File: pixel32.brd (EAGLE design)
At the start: 42 parts, among them CON1 DS1066-07M-SIDE, CON2 DS1066-07M-SIDE, IC1 STM32F030K6TX-LQFP32(7X7), IC2 ESDA6V1L, IC3 ST3485SOIC8, IC4 MC74VHC1GT125, IC5 MC74VHC1GT125, Q1 FDC6420C

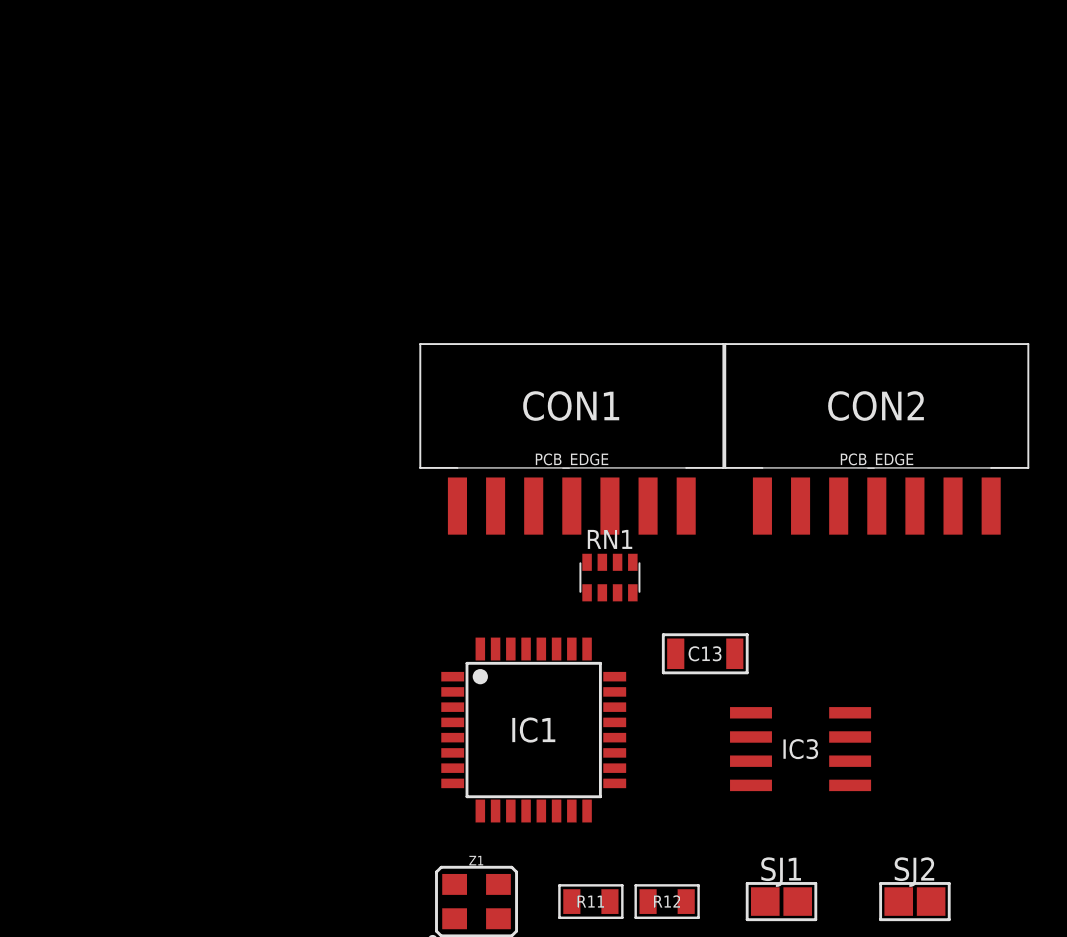
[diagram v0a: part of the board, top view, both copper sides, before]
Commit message: naming fixes pixel8 initial import
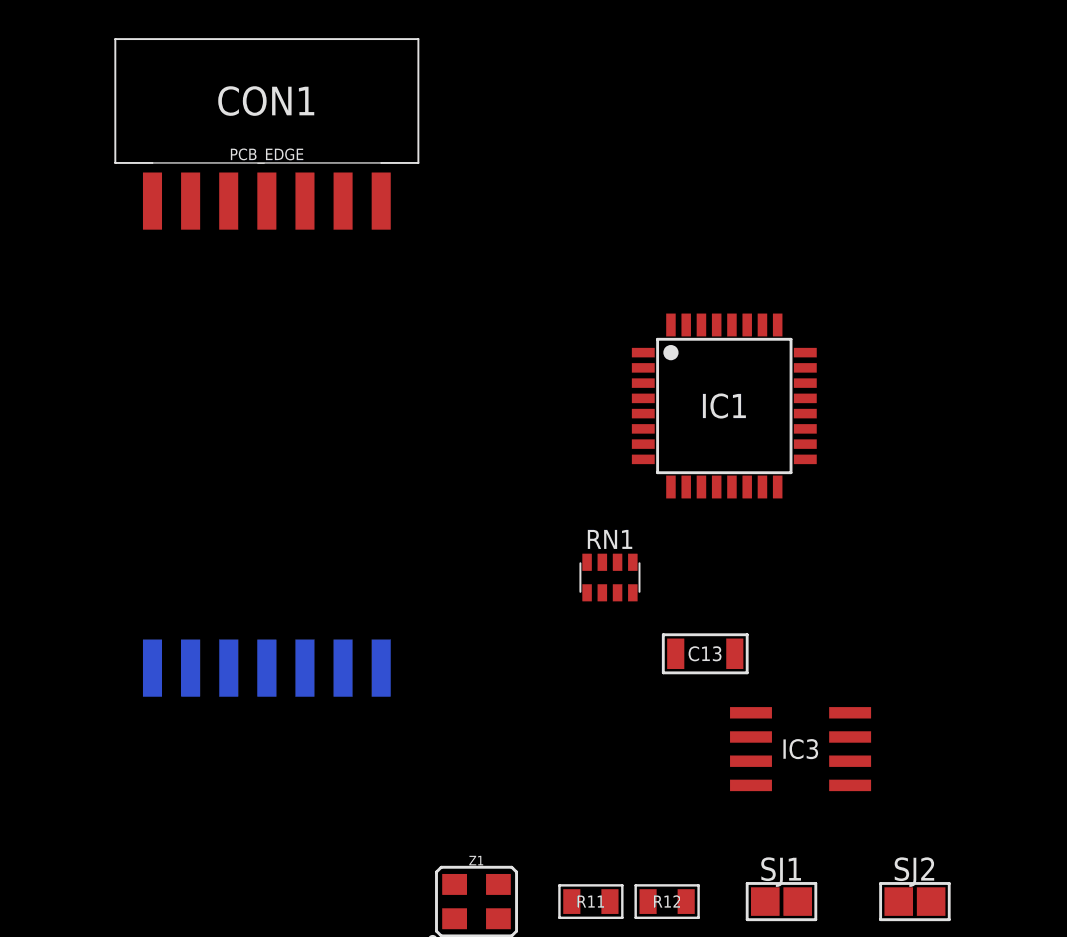
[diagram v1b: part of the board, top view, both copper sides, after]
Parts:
- moved CON2 33.2 mm to (-20.0, -30.0), flipped to the bottom, turned to 180 degrees
- moved CON1 22.6 mm to (-20.0, -5.00)
- moved IC1 19.7 mm to (4.00, -16.0)
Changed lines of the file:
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@@
 </autorouter>
 <elements>
-<element name="IC1" library="pixel_masterlib" package="LQFP32-7X7" value="STM32F030K6TX-LQFP32(7X7)" x="-6" y="-33">
-<attribute name="MANF" value="STMicroelectronics" x="-6" y="-19" size="1.778" layer="27" display="off"/>
-<attribute name="DIGIKEY#" value="497-14046-ND" x="-6" y="-19" size="1.778" layer="27" display="off"/>
-<attribute name="MANF#" value="STM32F030K6T6" x="-6" y="-19" size="1.778" layer="27" display="off"/>
+<element name="IC1" library="pixel_masterlib" package="LQFP32-7X7" value="STM32F030K6TX-LQFP32(7X7)" x="4" y="-16">
+<attribute name="MANF" value="STMicroelectronics" x="4" y="-2" size="1.778" layer="27" display="off"/>
+<attribute name="DIGIKEY#" value="497-14046-ND" x="4" y="-2" size="1.778" layer="27" display="off"/>
+<attribute name="MANF#" value="STM32F030K6T6" x="4" y="-2" size="1.778" layer="27" display="off"/>
 </element>
 <element name="C2" library="rc" package="C0603" value="100 nF" x="-6" y="-46">
@@
 <attribute name="MANF#" value="CX3225GB16000P0HPQCC" x="-8" y="-64" size="1.778" layer="27" display="off"/>
 </element>
-<element name="CON1" library="pixel_masterlib" package="DS1066-08M_SIDE" value="DS1066-07M-SIDE" x="-4" y="-21"/>
-<element name="CON2" library="pixel_masterlib" package="DS1066-08M_SIDE" value="DS1066-07M-SIDE" x="12" y="-21"/>
+<element name="CON1" library="pixel_masterlib" package="DS1066-08M_SIDE" value="DS1066-07M-SIDE" x="-20" y="-5"/>
+<element name="CON2" library="pixel_masterlib" package="DS1066-08M_SIDE" value="DS1066-07M-SIDE" x="-20" y="-30" rot="MR180"/>
 <element name="D1" library="pixel_masterlib" package="SC70_6L" value="SMF05C" x="-10" y="-53">
 <attribute name="MANF" value="Semtech Corporation" x="-9" y="-96" size="1.778" layer="27" display="off"/>
@@
 <wire x1="15.725" y1="-46" x2="12.725" y2="-46" width="0" layer="19" extent="1-1"/>
 <wire x1="18.725" y1="-46" x2="15.725" y2="-46" width="0" layer="19" extent="1-1"/>
-<wire x1="-1.75" y1="-35.8" x2="-1.275" y2="-46" width="0" layer="19" extent="1-1"/>
-<wire x1="-10.25" y1="-33.4" x2="-1.75" y2="-35.8" width="0" layer="19" extent="1-1"/>
-<wire x1="-10.25" y1="-30.2" x2="-10.25" y2="-33.4" width="0" layer="19" extent="1-1"/>
-<wire x1="10.6" y1="-32.095" x2="-1.75" y2="-35.8" width="0" layer="19" extent="1-1"/>
+<wire x1="8.25" y1="-18.8" x2="-1.275" y2="-46" width="0" layer="19" extent="1-1"/>
+<wire x1="-0.25" y1="-16.4" x2="8.25" y2="-18.8" width="0" layer="19" extent="1-1"/>
+<wire x1="-0.25" y1="-13.2" x2="-0.25" y2="-16.4" width="0" layer="19" extent="1-1"/>
+<wire x1="10.6" y1="-32.095" x2="8.25" y2="-18.8" width="0" layer="19" extent="1-1"/>
 </signal>
 <signal name="GND">
@@
 <wire x1="-5.725" y1="-50" x2="-6.725" y2="-46" width="0" layer="19" extent="1-1"/>
 <wire x1="0.275" y1="-50" x2="1.275" y2="-46" width="0" layer="19" extent="1-1"/>
-<wire x1="-3.2" y1="-37.25" x2="-7.85" y2="-42.9" width="0" layer="19" extent="1-1"/>
 <wire x1="10.6" y1="-35.905" x2="11.275" y2="-46" width="0" layer="19" extent="1-1"/>
 <wire x1="4.55" y1="-29" x2="10.6" y2="-35.905" width="0" layer="19" extent="1-1"/>
-<wire x1="2" y1="-21.25" x2="4.55" y2="-29" width="0" layer="19" extent="1-1"/>
-<wire x1="-8.8" y1="-28.75" x2="-3.2" y2="-37.25" width="0" layer="19" extent="1-1"/>
-<wire x1="18" y1="-21.25" x2="4.55" y2="-29" width="0" layer="19" extent="1-1"/>
+<wire x1="6.8" y1="-20.25" x2="4.55" y2="-29" width="0" layer="19" extent="1-1"/>
+<wire x1="1.2" y1="-11.75" x2="6.8" y2="-20.25" width="0" layer="19" extent="1-1"/>
+<wire x1="-14" y1="-29.75" x2="-10.15" y2="-41.1" width="0" layer="19" extent="1-16"/>
+<wire x1="-14" y1="-5.25" x2="1.2" y2="-11.75" width="0" layer="19" extent="1-1"/>
 </signal>
 <signal name="N$1">
@@
 <contactref element="Z1" pad="1"/>
 <wire x1="-10.15" y1="-42.9" x2="1.725" y2="-50" width="0" layer="19" extent="1-1"/>
-<wire x1="-10.25" y1="-31" x2="-10.15" y2="-42.9" width="0" layer="19" extent="1-1"/>
+<wire x1="-0.25" y1="-14" x2="-10.15" y2="-42.9" width="0" layer="19" extent="1-1"/>
 </signal>
 <signal name="N$3">
@@
 <contactref element="C10" pad="1"/>
 <contactref element="Z1" pad="3"/>
-<wire x1="-10.25" y1="-31.8" x2="-7.85" y2="-41.1" width="0" layer="19" extent="1-1"/>
+<wire x1="-0.25" y1="-14.8" x2="-7.85" y2="-41.1" width="0" layer="19" extent="1-1"/>
 <wire x1="3.275" y1="-50" x2="-7.85" y2="-41.1" width="0" layer="19" extent="1-1"/>
 </signal>
@@
 <contactref element="IC1" pad="8"/>
 <contactref element="IC3" pad="4"/>
-<wire x1="5.4" y1="-35.905" x2="-10.25" y2="-35.8" width="0" layer="19" extent="1-1"/>
+<wire x1="5.4" y1="-35.905" x2="-0.25" y2="-18.8" width="0" layer="19" extent="1-1"/>
 </signal>
 <signal name="DC-DC_FB">
@@
 <contactref element="IC1" pad="9"/>
 <contactref element="IC3" pad="1"/>
-<wire x1="5.4" y1="-32.095" x2="-8.8" y2="-37.25" width="0" layer="19" extent="1-1"/>
+<wire x1="5.4" y1="-32.095" x2="1.2" y2="-20.25" width="0" layer="19" extent="1-1"/>
 </signal>
 <signal name="CK">
@@
 <contactref element="IC1" pad="18"/>
 <contactref element="R4" pad="1"/>
-<wire x1="-1.75" y1="-35" x2="-39" y2="-65" width="0" layer="19" extent="1-1"/>
+<wire x1="8.25" y1="-18" x2="-39" y2="-65" width="0" layer="19" extent="1-1"/>
 </signal>
 <signal name="LED2_PWM">
@@
 <contactref element="IC5" pad="2"/>
 <wire x1="-9.025" y1="-52.35" x2="-19" y2="-57.3" width="0" layer="19" extent="1-1"/>
-<wire x1="-1.75" y1="-32.6" x2="-9.025" y2="-52.35" width="0" layer="19" extent="1-1"/>
-<wire x1="-1.6" y1="-25.8" x2="-1.75" y2="-32.6" width="0" layer="19" extent="1-1"/>
+<wire x1="8.25" y1="-15.6" x2="-9.025" y2="-52.35" width="0" layer="19" extent="1-1"/>
+<wire x1="-1.6" y1="-25.8" x2="8.25" y2="-15.6" width="0" layer="19" extent="1-1"/>
 </signal>
 <signal name="CLOCK">
@@
 <contactref element="IC4" pad="2"/>
 <wire x1="-9.025" y1="-53" x2="-15" y2="-57.3" width="0" layer="19" extent="1-1"/>
-<wire x1="-1.75" y1="-31.8" x2="-9.025" y2="-53" width="0" layer="19" extent="1-1"/>
-<wire x1="-2.4" y1="-25.8" x2="-1.75" y2="-31.8" width="0" layer="19" extent="1-1"/>
+<wire x1="8.25" y1="-14.8" x2="-9.025" y2="-53" width="0" layer="19" extent="1-1"/>
+<wire x1="-2.4" y1="-25.8" x2="8.25" y2="-14.8" width="0" layer="19" extent="1-1"/>
 </signal>
 <signal name="SYS_SWDIO">
@@
 <contactref element="CON1" pad="1"/>
 <contactref element="CON2" pad="1"/>
-<wire x1="6" y1="-21.25" x2="-10" y2="-21.25" width="0" layer="19" extent="1-1"/>
+<wire x1="-26" y1="-5.25" x2="-26" y2="-29.75" width="0" layer="19" extent="1-16"/>
 </signal>
 <signal name="RS485_B">
 <contactref element="CON1" pad="3"/>
 <contactref element="CON2" pad="3"/>
-<wire x1="10" y1="-21.25" x2="-6" y2="-21.25" width="0" layer="19" extent="1-1"/>
+<wire x1="-22" y1="-5.25" x2="-22" y2="-29.75" width="0" layer="19" extent="1-16"/>
 </signal>
 <signal name="RS485_A">
 <contactref element="CON1" pad="2"/>
 <contactref element="CON2" pad="2"/>
-<wire x1="8" y1="-21.25" x2="-8" y2="-21.25" width="0" layer="19" extent="1-1"/>
+<wire x1="-24" y1="-5.25" x2="-24" y2="-29.75" width="0" layer="19" extent="1-16"/>
 </signal>
 <signal name="N$2">
 <contactref element="CON1" pad="4"/>
 <contactref element="RN1" pad="8"/>
-<wire x1="-4" y1="-21.25" x2="-3.2" y2="-24.2" width="0" layer="19" extent="1-1"/>
+<wire x1="-3.2" y1="-24.2" x2="-20" y2="-5.25" width="0" layer="19" extent="1-1"/>
 </signal>
 <signal name="N$4">
 <contactref element="CON1" pad="5"/>
 <contactref element="RN1" pad="7"/>
-<wire x1="-2" y1="-21.25" x2="-2.4" y2="-24.2" width="0" layer="19" extent="1-1"/>
+<wire x1="-2.4" y1="-24.2" x2="-18" y2="-5.25" width="0" layer="19" extent="1-1"/>
 </signal>
 <signal name="N$5">
 <contactref element="CON1" pad="6"/>
 <contactref element="RN1" pad="6"/>
-<wire x1="0" y1="-21.25" x2="-1.6" y2="-24.2" width="0" layer="19" extent="1-1"/>
+<wire x1="-1.6" y1="-24.2" x2="-16" y2="-5.25" width="0" layer="19" extent="1-1"/>
 </signal>
 <signal name="DATA_IN">
 <contactref element="D1" pad="4"/>
 <contactref element="RN1" pad="1"/>
-<wire x1="-9.025" y1="-53.65" x2="-3.2" y2="-25.8" width="0" layer="19" extent="1-1"/>
+<wire x1="-3.2" y1="-25.8" x2="-9.025" y2="-53.65" width="0" layer="19" extent="1-1"/>
 </signal>
 <signal name="N$6">
 <contactref element="CON2" pad="4"/>
 <contactref element="RN2" pad="8"/>
-<wire x1="12" y1="-21.25" x2="-10.2" y2="-56.2" width="0" layer="19" extent="1-1"/>
+<wire x1="-20" y1="-29.75" x2="-10.2" y2="-56.2" width="0" layer="19" extent="1-16"/>
 </signal>
 <signal name="N$9">
 <contactref element="CON2" pad="5"/>
 <contactref element="RN2" pad="7"/>
-<wire x1="14" y1="-21.25" x2="-9.4" y2="-56.2" width="0" layer="19" extent="1-1"/>
+<wire x1="-18" y1="-29.75" x2="-9.4" y2="-56.2" width="0" layer="19" extent="1-16"/>
 </signal>
 <signal name="DE">
@@
 <contactref element="CON2" pad="6"/>
 <contactref element="RN2" pad="6"/>
-<wire x1="16" y1="-21.25" x2="-8.6" y2="-56.2" width="0" layer="19" extent="1-1"/>
+<wire x1="-16" y1="-29.75" x2="-8.6" y2="-56.2" width="0" layer="19" extent="1-16"/>
 </signal>
 <signal name="DATA_OUT">
@@
 <contactref element="IC1" pad="26"/>
 <contactref element="NRF24L01" pad="5"/>
-<wire x1="-4" y1="-28.75" x2="-42.7" y2="-93.73" width="0" layer="19" extent="1-1"/>
+<wire x1="6" y1="-11.75" x2="-42.7" y2="-93.73" width="0" layer="19" extent="1-1"/>
 </signal>
 <signal name="MISO">
 <contactref element="IC1" pad="27"/>
 <contactref element="NRF24L01" pad="7"/>
-<wire x1="-4.8" y1="-28.75" x2="-42.7" y2="-96.27" width="0" layer="19" extent="1-1"/>
+<wire x1="5.2" y1="-11.75" x2="-42.7" y2="-96.27" width="0" layer="19" extent="1-1"/>
 </signal>
 <signal name="MOSI">
 <contactref element="IC1" pad="28"/>
 <contactref element="NRF24L01" pad="6"/>
-<wire x1="-5.6" y1="-28.75" x2="-40.16" y2="-93.73" width="0" layer="19" extent="1-1"/>
+<wire x1="4.4" y1="-11.75" x2="-40.16" y2="-93.73" width="0" layer="19" extent="1-1"/>
 </signal>
 <signal name="NRF_IRQ">

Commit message: -added DC-DC
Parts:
- removed D1: SMF05C, pixel_masterlib:SC70_6L
- removed D2: SMAJ12A, masterlib:SMA
- added C15: 10 nF, rc:C0603
- added C16: 4.7 uF, rc:C0603
- added C17, C18, C23, C24: 100 nF, rc:C0603
- added C19, C20: (no value), rc:C0603
- added C21: 0.1uF, rc:C0603
- added C22: 1nF, rc:C1206
- added C25: 10uF 6.3V, rc:C1206
- added D3: B360B-SMB, eth_conv_master_lib:SMB
- added D5: SMAJ12A, masterlib:SMA
- added D6: CRS08-SOD123, eth_conv_master_lib:SOD123
- added IC6, IC7: MC74VHC1GT125, pixel_masterlib:SOT23-5
- added L2: 47UH, power_inductors:SDR0604
- added LED2, LED3: LED-0603, rc:LED0603
- added MODULE1: GW1584, ali_modules:GW1584
- added R10, R8: 22R, rc:R0805
- added R13: 10K, rc:R0805
- added R14: 2R, rc:R1206
- added R39, R40: 1K, rc:R0603
- added U$1: (no value), FMU_masterlib:SHIELD
- C1: value 100 nF -> 0.1uF
- C10: value (none) -> 1uF
- C11: value 0.1uF -> 1uF
- C13: value 1nF -> 100 nF; device rc:C1206 -> rc:C0603
- C14: value 10uF 6.3V -> 1 uF; device rc:C1206 -> rc:C0603
- C2, C3: value 100 nF -> 4.7u; device rc:C0603 -> rc:C1210
- C4: value 1 uF -> 10n
- C5: value 10 nF -> 47u 16V; device rc:C0603 -> rc:C1210
- C6: value 4.7 uF -> 47u 16V; device rc:C0603 -> rc:C1210
- C7, C8: value 100 nF -> 18pF
- C9: value (none) -> 4700p
- D4: value CRS08-SOD123 -> SMF05C; device eth_conv_master_lib:SOD123 -> pixel_masterlib:SC70_6L
- IC2: value ESDA6V1L -> TPS54260; device pixel_masterlib:SOT23 -> eth_conv_master_lib:MSOP10
- IC4: value MC74VHC1GT125 -> ESDA6V1L; device pixel_masterlib:SOT23-5 -> pixel_masterlib:SOT23
- IC5: value MC74VHC1GT125 -> 3.3; device pixel_masterlib:SOT23-5 -> gradus_mater_lib:SOT23-5L
- L1: value 47UH -> 3R3; device power_inductors:SDR0604 -> eth_conv_master_lib:SWPA6045S3R3N
- R1: value 60R -> 100K
- R2, R3: value 560R -> XXX
- R4: value 22R -> 18K 1%; device rc:R0805 -> rc:R0603
- R5: value 22R -> 60R; device rc:R0805 -> rc:R0603
- R6: value 10K -> 560R; device rc:R0805 -> rc:R0603
- R7: value 2R -> 560R; device rc:R1206 -> rc:R0603
- moved R4 94.1 mm to (14.4, 13.2), turned to 90 degrees
- moved IC5 93.1 mm to (18.4, 29.3), turned to 90 degrees
- moved L1 87.4 mm to (15.8, 18.7), turned to 90 degrees
- moved C1 84.8 mm to (9.03, 18.4)
- moved C10 83.0 mm to (19.2, 31.6), turned to 180 degrees
- moved C14 77.2 mm to (16.6, -69.1)
- moved NRF24L01 76.5 mm to (13.7, -32.2)
- moved C11 75.3 mm to (15.7, 29.3), turned to 270 degrees
- moved R7 73.9 mm to (23.7, -69.1)
- moved R6 67.5 mm to (21.4, -69.1)
- moved C5 67.0 mm to (21.1, 20.4), turned to 180 degrees
- moved C3 66.7 mm to (3.80, 20.4)
- moved R1 65.6 mm to (6.90, 13.2), turned to 90 degrees
- moved R2 65.2 mm to (8.40, 13.2), turned to 90 degrees
- moved IC2 64.9 mm to (9.03, 16.1)
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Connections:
- removed net N$11 (its old number): C13.P$1, SJ1.2
- removed net N$13 (its old number): Q1.1, R4.2
- removed net N$15 (its old number): Q1.6, R5.1
- removed net N$3: C10.1, IC1.3, Z1.3
- new net AA: C1.2, D3.C, IC2.10, L1.P$1
- new net FB: IC2.7, R2.2, R3.1
- new net LED1: R39.2
- new net LED2: R40.2
- new net N$16: R5.1, R9.2, SJ1.1
- new net N$2: C1.1, IC2.1
- new net N$20: Q1.1, R8.2
- new net N$21: Q1.3, R10.2, R13.2
- new net N$22: LED2.A, R39.1
- new net N$23: Q1.6, R10.1
- new net N$24: D6.C, L2.1, Q1.2
- new net N$4: C19.2, IC1.2, Z1.1
- new net N$5: C7.1, C8.1, IC2.8, R4.2
- new net N$6: C4.2, IC2.4
- new net N$9: C20.1, IC1.3, Z1.3
- net A: now also D5.A, IC4.2, R5.2, R6.2; no longer D2.A, IC2.2, R1.2, R3.2
- net B: now also D5.C, IC4.3, R7.1; no longer D2.C, IC2.3, R2.1
- net CLOCK: now also D4.5, IC6.2; no longer D1.5, IC4.2
- net CLOCK_BUFFERED: now also IC6.4; no longer IC4.4
- net DATA_IN: now also D4.4; no longer D1.4
- net GND: now also C10.1, C13.1, C14.1, C15.1, C16.1, C17.1, C18.1, C19.1, C20.2, C21.1, C22.P$2, C23.1, C24.1, C25.P$2, C7.2, C8.2, D3.A, D4.2, D6.A, IC2.9, IC2.TPAD, IC4.1, IC5.2, IC6.3, IC7.3, LED2.C, LED3.C, MODULE1.IN-@1, MODULE1.IN-@2, MODULE1.OUT-@1, MODULE1.OUT-@2, R1.1, R14.P$1, R2.1, R6.1; no longer C1.1, C10.2, C13.P$2, C14.P$2, C7.1, C8.1, D1.2, D4.A, IC2.1, IC4.3, IC5.3, R3.1, R7.P$1
- net LATCH: now also D4.6, IC7.2; no longer D1.6, IC5.2
- net LATCH_BUFFERED: now also IC7.4; no longer IC5.4
- net LED1_PWM: now also R8.1; no longer R4.1
- net N$1: now also LED3.A, R40.1; no longer C9.2, IC1.2, Z1.1
- net N$17: now also C22.P$1, SJ1.2; no longer D4.C, L1.1, Q1.2
- net N$7: now also IC2.5, R1.2; no longer Q1.3, R5.2, R6.2
- net N$8: now also C9.2, R4.1; no longer R1.1, R9.2, SJ1.1
- net VDD_12V: now also C10.2, C5.2, C6.2, IC5.1, IC5.3, L1.P$2, MODULE1.OUT+@1, MODULE1.OUT+@2, R13.1, R3.2; no longer R6.1
- net VDD_24V: now also C2.2, C3.2, IC2.2, MODULE1.IN+@1, MODULE1.IN+@2
- net VDD_3V3: now also C13.2, C14.2, C15.2, C16.2, C17.2, C18.2, C21.2, C23.2, C24.2, C25.P$1, IC6.5, IC7.5, R7.2; no longer C1.2, C14.P$1, C2.2, C3.2, C4.2, C5.2, C6.2, C7.2, C8.2, IC4.5, R2.2
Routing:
- net VDD_12V: track 0.00 -> 15.7 mm
- net N$5: track 0.00 -> 6.45 mm
- net FB: track 0.00 -> 6.26 mm
- net GND: track 0.00 -> 5.71 mm, vias 0 -> 30
- net N$6: track 0.00 -> 3.38 mm
- net VDD_24V: track 0.00 -> 2.26 mm
- net VDD_3V3: track 0.00 -> 1.51 mm
- net N$8: track 0.00 -> 1.47 mm
- net N$7: track 0.00 -> 1.24 mm
- added copper zone on layer 1, net AA
- added copper zone on layer 1, net N$2
- added copper zone on layer 1, net N$3
- added copper zone on layer 1, net VBAT
